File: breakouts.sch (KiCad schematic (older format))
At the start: 8 parts

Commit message: Sort remaining sections to sheets
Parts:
- added D? (x10): DIODE, symbol DIODE
- added P?: SMIRF, symbol CONN_6
- added P?: IO, symbol CONN_6
- added P?: SPI, symbol CONN_4
- added P?: UART, symbol CONN_4
- added P?: PCM, symbol CONN_4
- added P?: POWER, symbol CONN_4
- added P? (x2): CONN_5X2, symbol CONN_5X2
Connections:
- net +5V: now also P?.2 (P2)
- net COL_0: now also P?.1, P?.5
- net COL_11: now also P?.3, P?.9
- net COL_4: now also P?.3, P?.7
- net COL_5: now also P?.9
- net COL_6: now also P?.5
- net COL_7: now also P?.1, P?.7
- net GND: now also P?.1 (P1), P?.4
- net ROW_L4: now also D?.1 (A), D?.1 (A), D?.2 (K), D?.2 (K), P?.2, P?.4
- net ROW_L5: now also D?.1 (A), D?.1 (A), D?.1 (A), D?.2 (K), D?.2 (K), D?.2 (K), P?.10, P?.6, P?.8
- net ROW_R4: now also D?.1 (A), D?.1 (A), D?.2 (K), D?.2 (K), P?.2, P?.4
- net ROW_R5: now also D?.1 (A), D?.1 (A), D?.1 (A), D?.2 (K), D?.2 (K), D?.2 (K), P?.10, P?.6, P?.8
- net VCC: now also P?.3 (P3), P?.5
- new net W_MISO: P?.2 (P2)
- new net W_MOSI: P?.1 (P1)
- new net W_NCSB: P?.4 (P4)
- new net W_NCTS: P?.2 (P2), P?.6
- new net W_NRTS: P?.1, P?.3 (P3)
- new net W_PCMC: P?.3 (P3)
- new net W_PCMI: P?.1 (P1)
- new net W_PCMO: P?.2 (P2)
- new net W_PCMS: P?.4 (P4)
- new net W_PIO2: P?.1
- new net W_PIO3: P?.2
- new net W_PIO4: P?.3
- new net W_PIO5: P?.4
- new net W_PIO6: P?.5
- new net W_PIO7: P?.6
- new net W_RESET: P?.4 (P4)
- new net W_RXD: P?.1 (P1), P?.2
- new net W_SCLK: P?.3 (P3)
- new net W_TXD: P?.3, P?.4 (P4)

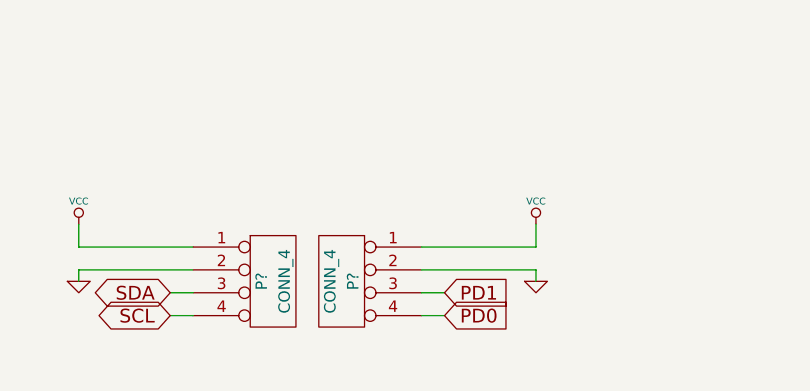
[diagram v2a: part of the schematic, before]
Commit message: Add MCP23018 interrupt connections
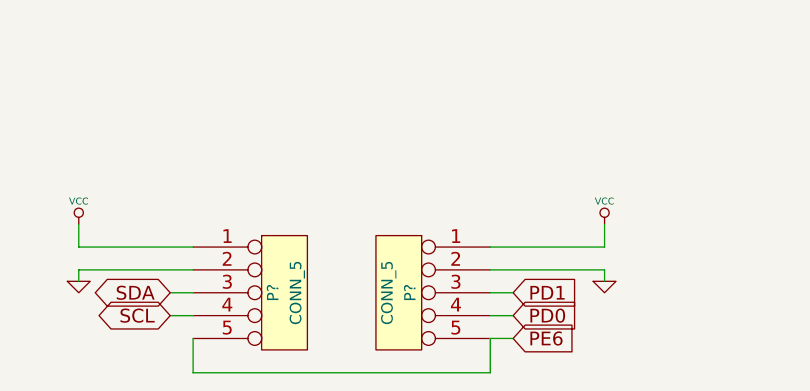
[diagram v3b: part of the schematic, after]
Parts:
- removed P? (x2): CONN_4, symbol CONN_4
- added P? (x2): CONN_5, symbol CONN_5
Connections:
- net GND: now also P?.2, P?.2
- net PD0: now also P?.4
- net PD1: now also P?.3
- net PE6: now also P?.5, P?.5
- net SCL: now also P?.4
- net SDA: now also P?.3
- net VCC: now also P?.1, P?.1
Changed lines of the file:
@@
 Text GLabel 2850 6100 0    60   BiDi ~ 0
 SDA
-Text GLabel 4050 6200 2    60   Input ~ 0
+Text GLabel 4350 6200 2    60   Input ~ 0
 PD0
-Text GLabel 4050 6100 2    60   Input ~ 0
+Text GLabel 4350 6100 2    60   Input ~ 0
 PD1
 $Comp
@@
 L GND #PWR?
 U 1 1 54E556E6
-P 4450 6050
-F 0 "#PWR?" H 4450 6050 30  0001 C CNN
-F 1 "GND" H 4450 5980 30  0001 C CNN
-F 2 "" H 4450 6050 60  0000 C CNN
-F 3 "" H 4450 6050 60  0000 C CNN
-	1    4450 6050
+P 4750 6050
+F 0 "#PWR?" H 4750 6050 30  0001 C CNN
+F 1 "GND" H 4750 5980 30  0001 C CNN
+F 2 "" H 4750 6050 60  0000 C CNN
+F 3 "" H 4750 6050 60  0000 C CNN
+	1    4750 6050
 	1    0    0    -1
 $EndComp
@@
 L VCC #PWR?
 U 1 1 54E556F2
-P 4450 5800
-F 0 "#PWR?" H 4450 5900 30  0001 C CNN
-F 1 "VCC" H 4450 5900 30  0000 C CNN
-F 2 "" H 4450 5800 60  0000 C CNN
-F 3 "" H 4450 5800 60  0000 C CNN
-	1    4450 5800
-	1    0    0    -1
-$EndComp
-$Comp
-L CONN_4 P?
-U 1 1 54E556F8
-P 3300 6050
-F 0 "P?" V 3250 6050 50  0000 C CNN
-F 1 "CONN_4" V 3350 6050 50  0000 C CNN
-F 2 "" H 3300 6050 60  0000 C CNN
-F 3 "" H 3300 6050 60  0000 C CNN
-	1    3300 6050
-	1    0    0    -1
-$EndComp
-$Comp
-L CONN_4 P?
-U 1 1 54E556FF
-P 3600 6050
-F 0 "P?" V 3550 6050 50  0000 C CNN
-F 1 "CONN_4" V 3650 6050 50  0000 C CNN
-F 2 "" H 3600 6050 60  0000 C CNN
-F 3 "" H 3600 6050 60  0000 C CNN
-	1    3600 6050
-	-1   0    0    -1
+P 4750 5800
+F 0 "#PWR?" H 4750 5900 30  0001 C CNN
+F 1 "VCC" H 4750 5900 30  0000 C CNN
+F 2 "" H 4750 5800 60  0000 C CNN
+F 3 "" H 4750 5800 60  0000 C CNN
+	1    4750 5800
+	1    0    0    -1
 $EndComp
 Wire Wire Line
@@
 	2850 6200 2950 6200
 Wire Wire Line
-	4050 6100 3950 6100
-Wire Wire Line
-	3950 6200 4050 6200
-Wire Wire Line
-	3950 6000 4450 6000
-Wire Wire Line
-	4450 6000 4450 6050
-Wire Wire Line
-	3950 5900 4450 5900
-Wire Wire Line
-	4450 5900 4450 5800
+	4350 6100 4250 6100
+Wire Wire Line
+	4250 6200 4350 6200
+Wire Wire Line
+	4250 6000 4750 6000
+Wire Wire Line
+	4750 6000 4750 6050
+Wire Wire Line
+	4250 5900 4750 5900
+Wire Wire Line
+	4750 5900 4750 5800
 $Comp
 L +5V #PWR?
@@
 Text GLabel 5400 2000 2    60   Input ~ 0
 COL_11
+$Comp
+L CONN_5 P?
+U 1 1 54E803DF
+P 3350 6100
+F 0 "P?" V 3300 6100 50  0000 C CNN
+F 1 "CONN_5" V 3400 6100 50  0000 C CNN
+F 2 "" H 3350 6100 60  0000 C CNN
+F 3 "" H 3350 6100 60  0000 C CNN
+	1    3350 6100
+	1    0    0    -1
+$EndComp
+$Comp
+L CONN_5 P?
+U 1 1 54E80505
+P 3850 6100
+F 0 "P?" V 3800 6100 50  0000 C CNN
+F 1 "CONN_5" V 3900 6100 50  0000 C CNN
+F 2 "" H 3850 6100 60  0000 C CNN
+F 3 "" H 3850 6100 60  0000 C CNN
+	1    3850 6100
+	-1   0    0    -1
+$EndComp
+Text GLabel 4350 6300 2    60   Input ~ 0
+PE6
+Wire Wire Line
+	4350 6300 4250 6300
+Wire Wire Line
+	4250 6300 4250 6450
+Wire Wire Line
+	4250 6450 2950 6450
+Wire Wire Line
+	2950 6450 2950 6300
 $EndSCHEMATC
